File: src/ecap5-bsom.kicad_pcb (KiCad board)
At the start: 6 copper layers, 69.6 x 30 mm, 193 parts, among them J13 DDR4_SODIMM_Board, U1 TPS565242DRDR, U10 IS42S16160J-*BL, U11 IS43DR86400E, U12 ASFC4G31M-51*, U2 TPS562202DRLR, U3 TPS562202DRLR, U4 TPS562202DRLR, U5 LM3880MF*-1AA, U6 LFE5U-85F-*BG756*, U7 XLH335040.000000I, U8 W25Q128JVPIQ, U9 IS61WV25616BLL-*BLI

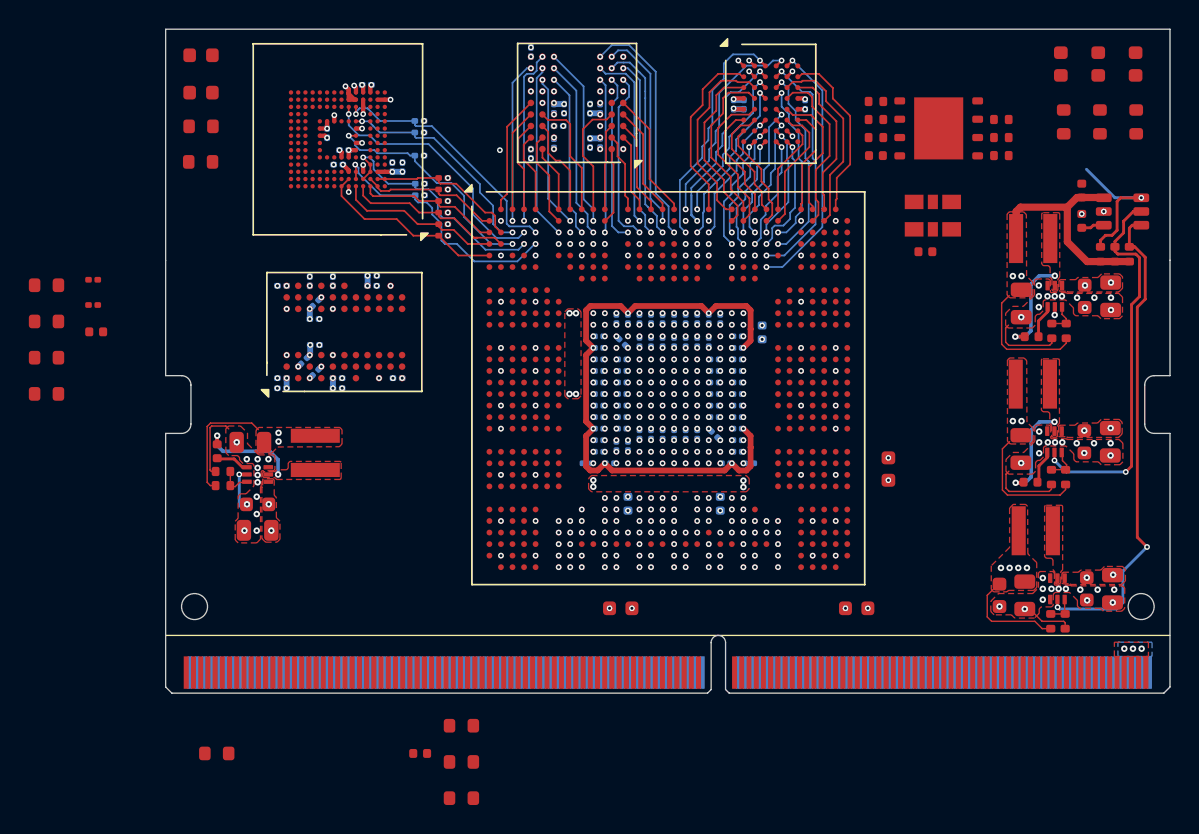
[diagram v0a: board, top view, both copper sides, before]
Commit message: Start routing DDR2 data lanes
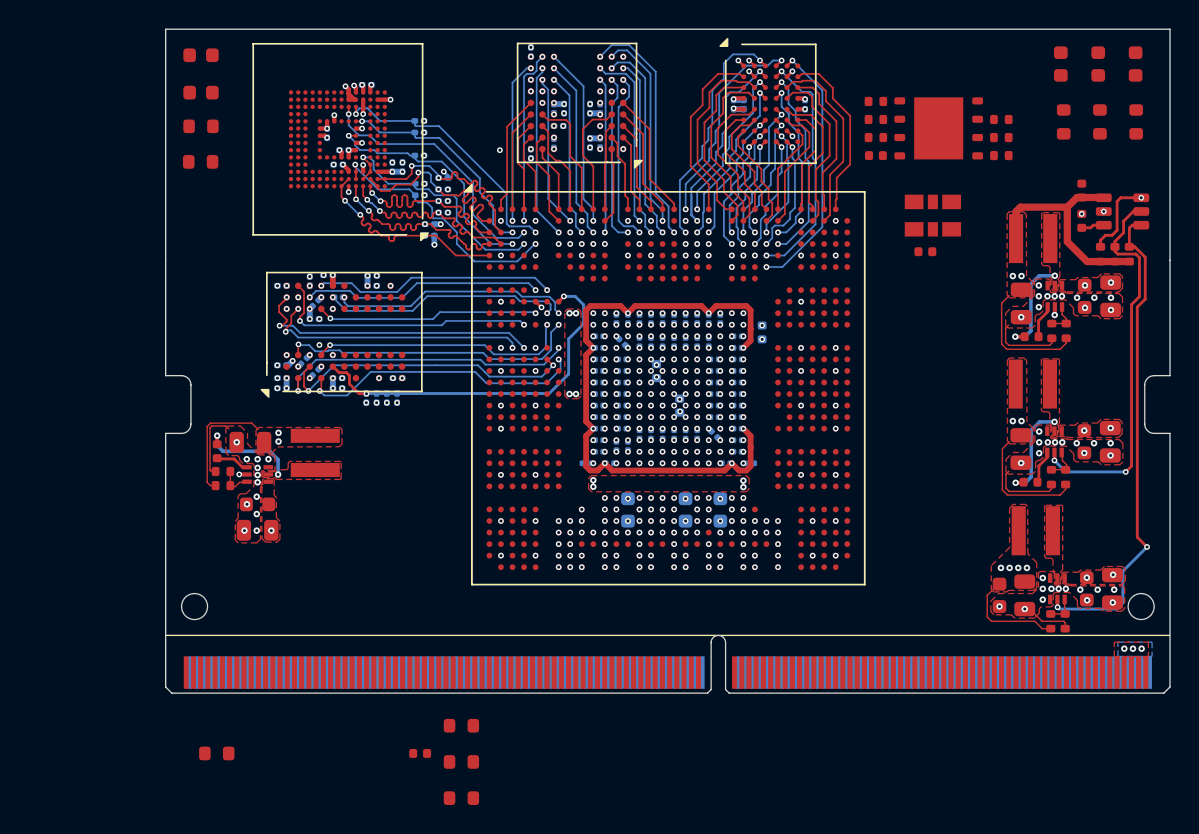
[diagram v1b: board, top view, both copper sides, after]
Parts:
- removed C120: 100n, Capacitor_SMD:C_0201_0603Metric
- removed C122: 0.47u, Capacitor_SMD:C_0402_1005Metric
- removed R25: 51, Resistor_SMD:R_0603_1608Metric
- added C138: 1u, Capacitor_SMD:C_0201_0603Metric, B.Cu at (109.1, 50.6)
- C121: value 0.47u -> 1u; moved to B.Cu
- C33, C34, C35, R1, R2, R3, R35, R38, R4: moved to B.Cu
- R23, R24: value 1k -> 1k 1%; footprint Resistor_SMD:R_0603_1608Metric -> Resistor_SMD:R_0201_0603Metric; moved to B.Cu
- R26: value 51 -> 100; footprint Resistor_SMD:R_0603_1608Metric -> Resistor_SMD:R_0201_0603Metric; moved to B.Cu
- moved R23 25.5 mm to (111.3, 50.6), turned to 90 degrees
- moved R24 24.2 mm to (110.5, 50.6), turned to -90 degrees
- moved R26 21.3 mm to (107.2, 43.6)
- moved C121 20.7 mm to (109.8, 50.6), turned to -90 degrees
- moved C35 13.7 mm to (131.2, 58.4), turned to -90 degrees
- moved C34 12.0 mm to (133.7, 58.4), turned to -90 degrees
- moved C137 9.40 mm to (129.2, 48.8)
- moved C136 7.36 mm to (130.8, 51.2), turned to 90 degrees
- moved C33 6.84 mm to (127.3, 58.4), turned to -90 degrees
- moved C116 2.68 mm to (103.3, 48.4), turned to 180 degrees
- moved R38 0.94 mm to (113.5, 39.4)
- moved R3 0.94 mm to (113.5, 38.6)
- moved C105 0.53 mm to (106.5, 42.1), turned to 180 degrees
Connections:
- net /FPGA Bank 7/CLK renamed /FPGA Bank 7/EMMC.CLK
- net /FPGA Bank 7/CMD renamed /FPGA Bank 7/EMMC.CMD
- net /FPGA Bank 7/DS renamed /FPGA Bank 7/EMMC.DS
- net /FPGA Bank 7/~{RST} renamed /FPGA Bank 7/EMMC.~{RST}
- R26 pad 1: /FPGA Bank 7/CK -> /FPGA Bank 7/DDR2.CK+
- R26 pad 2: Net-(C122-Pad1) -> /FPGA Bank 7/DDR2.CK-
- U11 pad A8: /DDR2/~{DQS} -> /FPGA Bank 7/DDR2.DQS-
- U11 pad B3: /DDR2/DM -> /FPGA Bank 7/DDR2.DM
- U11 pad B7: /DDR2/DQS -> /FPGA Bank 7/DDR2.DQS+
- U11 pad E8: /FPGA Bank 7/CK -> /FPGA Bank 7/DDR2.CK+
- U11 pad F2: /FPGA Bank 7/CKE -> /DDR2/CKE
- U11 pad F3: /FPGA Bank 7/~{WE} -> /DDR2/~{WE}
- U11 pad F7: /FPGA Bank 7/~{RAS} -> /DDR2/~{RAS}
- U11 pad F8: /FPGA Bank 7/~{CK} -> /FPGA Bank 7/DDR2.CK-
- U11 pad F9: /FPGA Bank 7/ODT -> /DDR2/ODT
- U11 pad G7: /FPGA Bank 7/~{CAS} -> /DDR2/~{CAS}
- U11 pad G8: /FPGA Bank 7/~{CS} -> /DDR2/~{CS}
- U6 pad E3: /DDR2/A2 -> unconnected-(U6H-PL20B/LDQ17-PadE3)
- U6 pad E4: /DDR2/DQ6 -> unconnected-(U6H-PL14B/LDQ17-PadE4)
- U6 pad F1: /DDR2/A5 -> unconnected-(U6H-PL23C/LDQ29-PadF1)
- U6 pad F2: /DDR2/A4 -> unconnected-(U6H-PL23A/LDQ29-PadF2)
- U6 pad F3: /DDR2/A0 -> unconnected-(U6H-PL20A/LDQ17-PadF3)
- U6 pad F4: /DDR2/DQ5 -> unconnected-(U6H-PL14C/LDQ17-PadF4)
- U6 pad F5: /DDR2/DQ7 -> unconnected-(U6H-PL14D/LDQ17-PadF5)
- U6 pad H1: /DDR2/A7 -> unconnected-(U6H-PL23D/LDQ29-PadH1)
- U6 pad H2: /DDR2/A8 -> unconnected-(U6H-PL26A/LDQ29-PadH2)
- U6 pad H3: /DDR2/A10 -> unconnected-(U6H-PL26B/LDQ29-PadH3)
- U6 pad H5: /FPGA Bank 7/~{CK} -> /DDR2/DQ0
- U6 pad H6: /FPGA Bank 7/~{WE} -> /DDR2/DQ5
- U6 pad J1: /DDR2/BA0 -> unconnected-(U6H-PL29B/LDQSN29-PadJ1)
- U6 pad J3: /DDR2/A9 -> unconnected-(U6H-PL26C/LDQ29-PadJ3)
- U6 pad J4: /FPGA Bank 7/~{CAS} -> unconnected-(U6H-PL32C/LDQ29-PadJ4)
- U6 pad J6: /FPGA Bank 7/CKE -> unconnected-(U6H-PL35D/LDQ41-PadJ6)
- U6 pad J7: /FPGA Bank 7/CK -> /DDR2/VREF
- U6 pad K1: /DDR2/A13 -> unconnected-(U6H-PL29C/LDQ29-PadK1)
- U6 pad K2: /DDR2/A12 -> unconnected-(U6H-PL29A/LDQS29-PadK2)
- U6 pad K3: /DDR2/A11 -> unconnected-(U6H-PL26D/LDQ29-PadK3)
- U6 pad K4: /FPGA Bank 7/~{RAS} -> unconnected-(U6H-PL32D/LDQ29-PadK4)
- U6 pad K5: unconnected-(U6H-PL38C/LDQ41-PadK5) -> /DDR2/DQ2
- U6 pad K6: unconnected-(U6H-PL38A/LDQ41-PadK6) -> /FPGA Bank 7/DDR2.CK+
- U6 pad K7: unconnected-(U6H-PL38B/LDQ41-PadK7) -> /FPGA Bank 7/DDR2.CK-
- U6 pad L1: /DDR2/BA1 -> unconnected-(U6H-PL29D/LDQ29-PadL1)
- U6 pad L2: /FPGA Bank 7/~{CS} -> unconnected-(U6H-PL32A/LDQ29-PadL2)
- U6 pad L3: /FPGA Bank 7/ODT -> unconnected-(U6H-PL32B/LDQ29-PadL3)
- U6 pad L4: unconnected-(U6H-PL38D/LDQ41-PadL4) -> /DDR2/DQ7
- U6 pad L6: unconnected-(U6H-PL41D/LDQ41-PadL6) -> /DDR2/DQ3
- U6 pad L7: unconnected-(U6H-PL41C/GR_PCLK7_0/LDQ41-PadL7) -> /FPGA Bank 7/DDR2.DM
- U6 pad N3: unconnected-(U6H-PL41A/GR_PCLK7_1/LDQS41-PadN3) -> /FPGA Bank 7/DDR2.DQS+
- U6 pad N4: unconnected-(U6H-PL41B/LDQSN41-PadN4) -> /FPGA Bank 7/DDR2.DQS-
- U6 pad N7: unconnected-(U6H-PL44B/PCLKC7_1/LDQ41-PadN7) -> /DDR2/DQ6
- U6 pad P6: unconnected-(U6H-PL44C/PCLKT7_0/LDQ41-PadP6) -> /DDR2/DQ1
- U6 pad P7: unconnected-(U6H-PL44D/PCLKC7_0/LDQ41-PadP7) -> /DDR2/DQ4
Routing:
- net /DDR2/VREF: track 0.00 -> 25.4 mm, vias 0 -> 2
- net /DDR2/DQ6: track 0.00 -> 21.1 mm, vias 0 -> 2
- net /FPGA Bank 7/DDR2.DM: track 0.00 -> 20.9 mm, vias 0 -> 2
- net /DDR2/DQ1: track 0.00 -> 20.9 mm, vias 0 -> 2
- net /FPGA Bank 7/DDR2.DQS-: track 0.00 -> 20.3 mm, vias 0 -> 3
- net /DDR2/DQ4: track 0.00 -> 19.9 mm, vias 0 -> 2
- net /DDR2/DQ7: track 0.00 -> 18.6 mm, vias 0 -> 2
- net /FPGA Bank 7/DDR2.DQS+: track 0.00 -> 18.4 mm, vias 0 -> 3
- net /DDR2/DQ3: track 0.00 -> 18.0 mm, vias 0 -> 2
- net /FPGA Bank 7/DDR2.CK+: track 0.00 -> 16.8 mm, vias 0 -> 2
- net /DDR2/DQ5: track 0.00 -> 16.7 mm, vias 0 -> 2
- net /DDR2/DQ0: track 0.00 -> 16.7 mm, vias 0 -> 2
- net /FPGA Bank 7/DDR2.CK-: track 0.00 -> 16.6 mm, vias 0 -> 2
- net /DDR2/DQ2: track 0.00 -> 15.4 mm, vias 0 -> 2
- net /Power/en_1v8: track 13.0 -> 6.20 mm
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
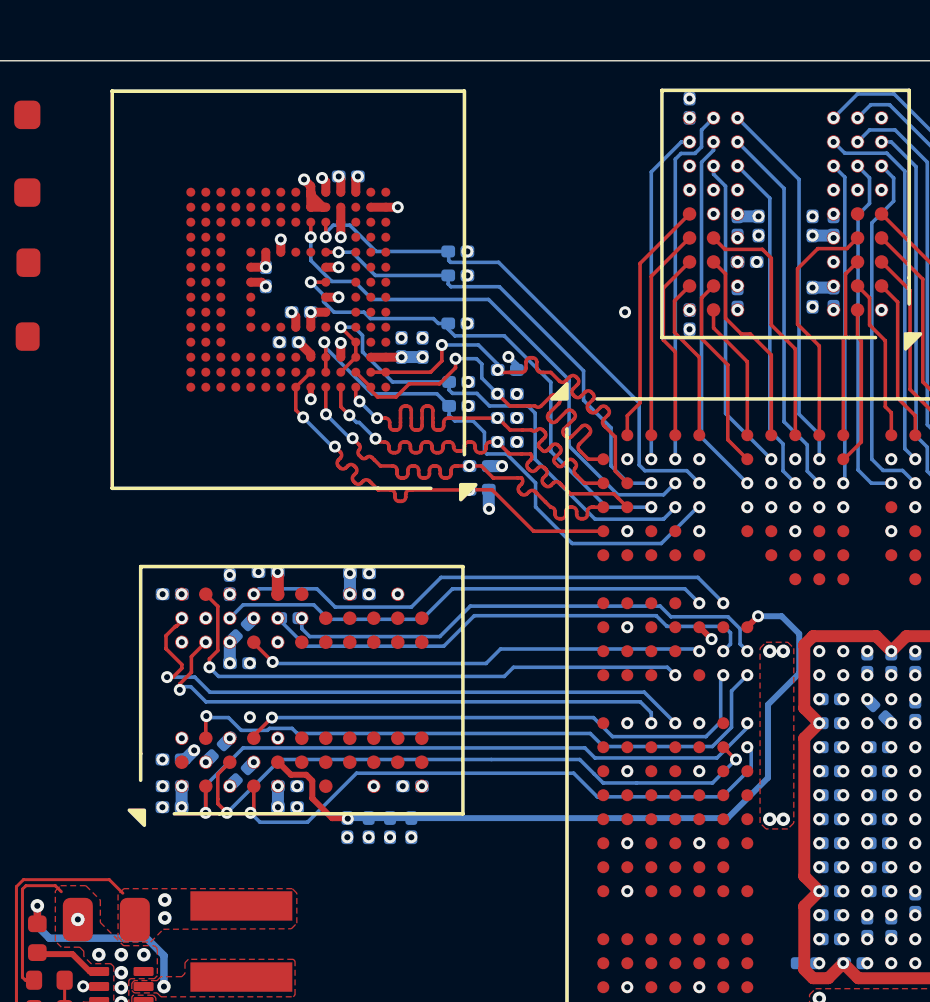
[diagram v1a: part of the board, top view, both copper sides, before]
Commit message: Use 0402 resistors instead of 0201 for emmc termination
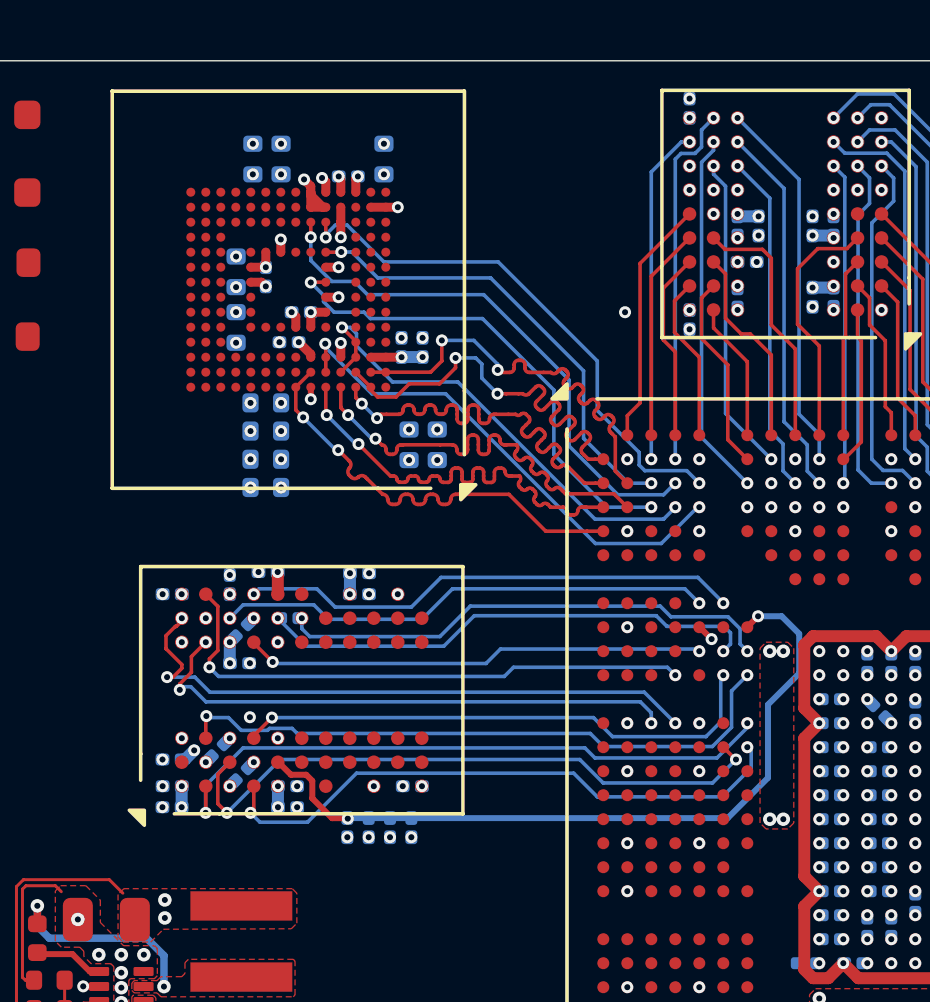
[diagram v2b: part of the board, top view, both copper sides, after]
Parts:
- R1, R2, R3, R35, R36, R37, R38, R39, R4, R40, R42: footprint Resistor_SMD:R_0201_0603Metric -> Resistor_SMD:R_0402_1005Metric
- moved R42 8.76 mm to (106.0, 28.3), turned to 90 degrees
- moved R36 8.28 mm to (105.4, 32.1), turned to -90 degrees
- moved R1 8.07 mm to (106.4, 36.5), turned to 0 degrees
- moved R2 8.06 mm to (106.4, 37.4), turned to 0 degrees
- moved R37 7.87 mm to (105.4, 34.0), turned to -90 degrees
- moved R3 7.12 mm to (106.4, 38.4), turned to 0 degrees
- moved R38 7.11 mm to (106.4, 39.3), turned to 0 degrees
- moved R39 6.65 mm to (106.9, 28.3), turned to -90 degrees
- moved R40 4.60 mm to (110.3, 28.3), turned to -90 degrees
- moved R4 4.12 mm to (111.2, 37.9), turned to 90 degrees
- moved R35 2.88 mm to (112.1, 37.9), turned to 90 degrees
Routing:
- net /FPGA Bank 7/EMMC.DS: track 16.5 -> 20.7 mm, vias 2 -> 3
- net /FPGA Bank 7/EMMC.IO3: track 14.8 -> 18.1 mm, vias 2 -> 3
- net /FPGA Bank 7/EMMC.~{RST}: track 15.5 -> 18.7 mm, vias 2 -> 3
- net /FPGA Bank 7/EMMC.IO0: track 14.8 -> 17.8 mm
- net /FPGA Bank 7/EMMC.IO5: track 17.3 -> 20.1 mm, vias 2 -> 3
- net /FPGA Bank 7/EMMC.IO2: track 14.8 -> 17.6 mm
- net /FPGA Bank 7/EMMC.IO4: track 14.8 -> 17.5 mm, vias 2 -> 3
- net /FPGA Bank 7/EMMC.CMD: track 18.1 -> 20.7 mm, vias 2 -> 3
- net /FPGA Bank 7/EMMC.IO1: track 14.8 -> 17.1 mm
- net /FPGA Bank 7/EMMC.IO7: track 14.9 -> 17.1 mm
- net /FPGA Bank 7/EMMC.IO6: track 17.9 -> 20.0 mm, vias 2 -> 3
- net +1V8: track 17.6 -> 15.9 mm

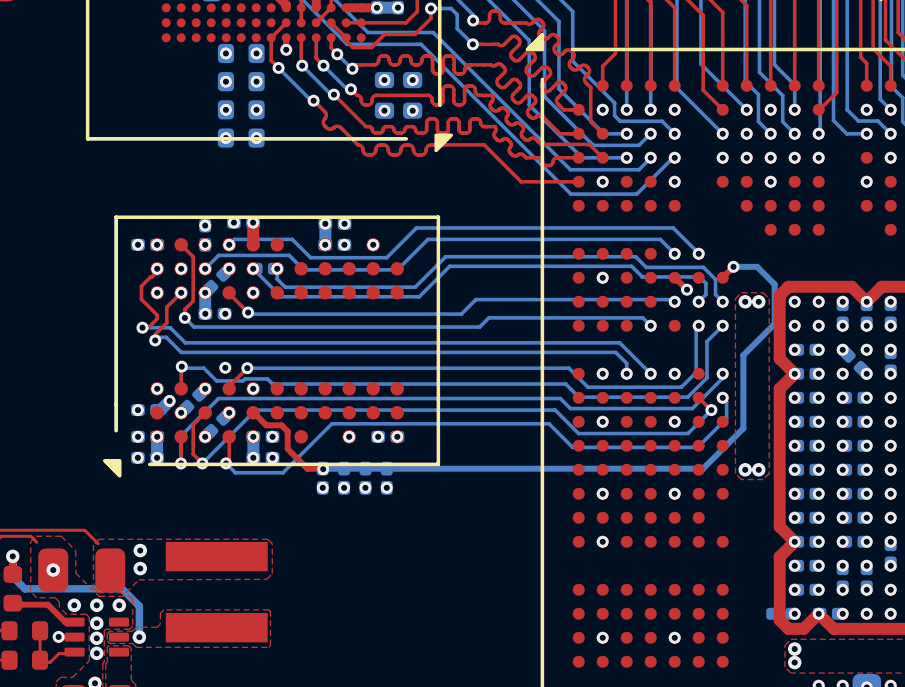
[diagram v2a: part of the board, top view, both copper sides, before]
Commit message: Route signals from DDR2 to FPGA bank
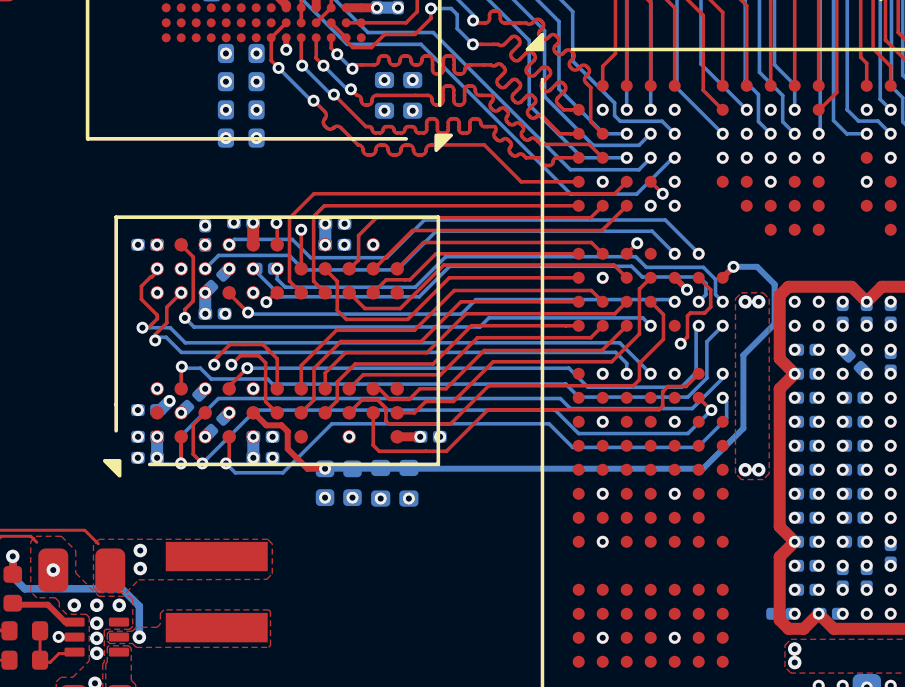
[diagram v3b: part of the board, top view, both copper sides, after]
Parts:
- C121, C138: footprint Capacitor_SMD:C_0201_0603Metric -> Capacitor_SMD:C_0402_1005Metric
- R23, R24: footprint Resistor_SMD:R_0201_0603Metric -> Resistor_SMD:R_0402_1005Metric
- moved C108 1.41 mm to (112.7, 49.3), turned to 0 degrees
- moved R23 0.76 mm to (112.0, 50.8)
- moved R24 0.53 mm to (111.0, 50.8)
- moved C121 0.33 mm to (110.1, 50.8)
- moved C138 0.18 mm to (109.2, 50.8)
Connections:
- U11 pad F2: /DDR2/CKE -> /FPGA Bank 7/DDR2.CKE
- U11 pad F3: /DDR2/~{WE} -> /FPGA Bank 7/DDR2.~{WE}
- U11 pad F7: /DDR2/~{RAS} -> /FPGA Bank 7/~{RAS}
- U11 pad F9: /DDR2/ODT -> /FPGA Bank 7/DDR2.ODT
- U11 pad G7: /DDR2/~{CAS} -> /FPGA Bank 7/DDR2.~{CAS}
- U11 pad G8: /DDR2/~{CS} -> /FPGA Bank 7/DDR2.~{CS}
- U6 pad E3: unconnected-(U6H-PL20B/LDQ17-PadE3) -> /FPGA Bank 7/DDR2.~{CAS}
- U6 pad E4: unconnected-(U6H-PL14B/LDQ17-PadE4) -> /FPGA Bank 7/DDR2.ODT
- U6 pad F1: unconnected-(U6H-PL23C/LDQ29-PadF1) -> /DDR2/A1
- U6 pad F2: unconnected-(U6H-PL23A/LDQ29-PadF2) -> /DDR2/A4
- U6 pad F3: unconnected-(U6H-PL20A/LDQ17-PadF3) -> /DDR2/A8
- U6 pad F4: unconnected-(U6H-PL14C/LDQ17-PadF4) -> /FPGA Bank 7/DDR2.~{CS}
- U6 pad F5: unconnected-(U6H-PL14D/LDQ17-PadF5) -> /FPGA Bank 7/~{RAS}
- U6 pad H1: unconnected-(U6H-PL23D/LDQ29-PadH1) -> /DDR2/A11
- U6 pad H2: unconnected-(U6H-PL26A/LDQ29-PadH2) -> /DDR2/A13
- U6 pad H3: unconnected-(U6H-PL26B/LDQ29-PadH3) -> /FPGA Bank 7/DDR2.~{WE}
- U6 pad J1: unconnected-(U6H-PL29B/LDQSN29-PadJ1) -> /DDR2/A0
- U6 pad J3: unconnected-(U6H-PL26C/LDQ29-PadJ3) -> /DDR2/A6
- U6 pad J4: unconnected-(U6H-PL32C/LDQ29-PadJ4) -> /DDR2/A12
- U6 pad J6: unconnected-(U6H-PL35D/LDQ41-PadJ6) -> /FPGA Bank 7/DDR2.CKE
- U6 pad K1: unconnected-(U6H-PL29C/LDQ29-PadK1) -> /DDR2/BA0
- U6 pad K2: unconnected-(U6H-PL29A/LDQS29-PadK2) -> /DDR2/BA1
- U6 pad K3: unconnected-(U6H-PL26D/LDQ29-PadK3) -> /DDR2/A2
- U6 pad K4: unconnected-(U6H-PL32D/LDQ29-PadK4) -> /DDR2/A3
- U6 pad L1: unconnected-(U6H-PL29D/LDQ29-PadL1) -> /DDR2/A10
- U6 pad L2: unconnected-(U6H-PL32A/LDQ29-PadL2) -> /DDR2/A5
- U6 pad L3: unconnected-(U6H-PL32B/LDQ29-PadL3) -> /DDR2/A9
- U6 pad N6: unconnected-(U6H-PL44A/PCLKT7_1/LDQ41-PadN6) -> /DDR2/A7
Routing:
- net /FPGA Bank 7/DDR2.CKE: track 0.00 -> 21.5 mm, vias 0 -> 2
- net /FPGA Bank 7/DDR2.~{WE}: track 0.00 -> 20.5 mm, vias 0 -> 2
- net /FPGA Bank 7/~{RAS}: track 0.00 -> 15.4 mm, vias 0 -> 2
- net /FPGA Bank 7/DDR2.ODT: track 0.00 -> 14.6 mm, vias 0 -> 2
- net /FPGA Bank 7/DDR2.~{CAS}: track 0.00 -> 14.4 mm
- net /DDR2/A3: track 0.00 -> 14.1 mm
- net /DDR2/A7: track 0.00 -> 13.4 mm
- net /FPGA Bank 7/DDR2.~{CS}: track 0.00 -> 13.3 mm, vias 0 -> 2
- net /DDR2/BA1: track 0.00 -> 12.0 mm
- net /DDR2/A1: track 0.00 -> 11.7 mm
- net /DDR2/A2: track 0.00 -> 11.6 mm
- net /DDR2/BA0: track 0.00 -> 11.4 mm
- net /DDR2/A12: track 0.00 -> 11.2 mm
- net /DDR2/A0: track 0.00 -> 10.3 mm
- net /DDR2/A6: track 0.00 -> 10.2 mm
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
